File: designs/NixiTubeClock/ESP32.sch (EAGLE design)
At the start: 19 parts, among them IC6 ESP32-WROVER-B

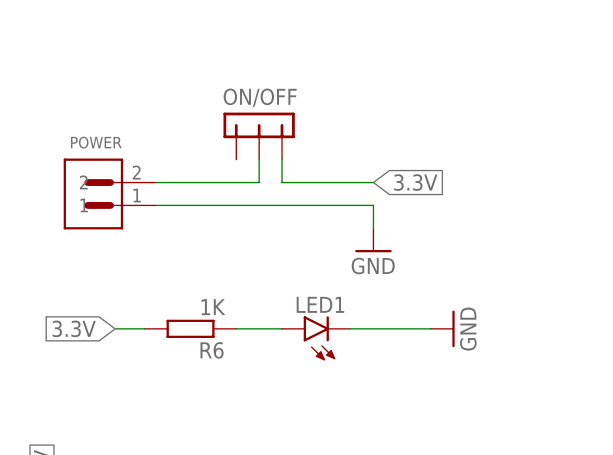
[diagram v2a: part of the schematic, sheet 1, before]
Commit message: integrated T/H sensor
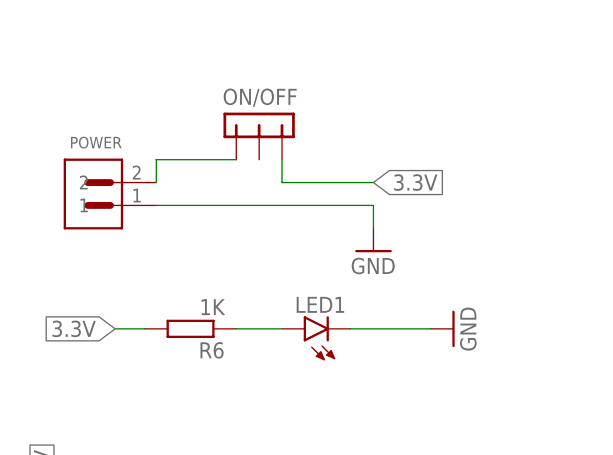
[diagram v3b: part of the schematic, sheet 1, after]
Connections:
- net N$1: now also ON/OFF.3; no longer ON/OFF.2
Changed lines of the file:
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@@
 <segment>
 <pinref part="POWER" gate="G$1" pin="2"/>
-<pinref part="ON/OFF" gate="G$1" pin="2"/>
-<wire x1="96.52" y1="247.65" x2="107.95" y2="247.65" width="0.1524" layer="91"/>
-<wire x1="107.95" y1="247.65" x2="107.95" y2="250.19" width="0.1524" layer="91"/>
+<pinref part="ON/OFF" gate="G$1" pin="3"/>
+<wire x1="96.52" y1="247.65" x2="96.52" y2="250.19" width="0.1524" layer="91"/>
+<wire x1="96.52" y1="250.19" x2="105.41" y2="250.19" width="0.1524" layer="91"/>
 </segment>
 </net>
